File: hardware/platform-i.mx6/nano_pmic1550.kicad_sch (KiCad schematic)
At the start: 57 parts, among them J5 CAN, Q1 2SK3018, U4 AP1509, U6 PF1550

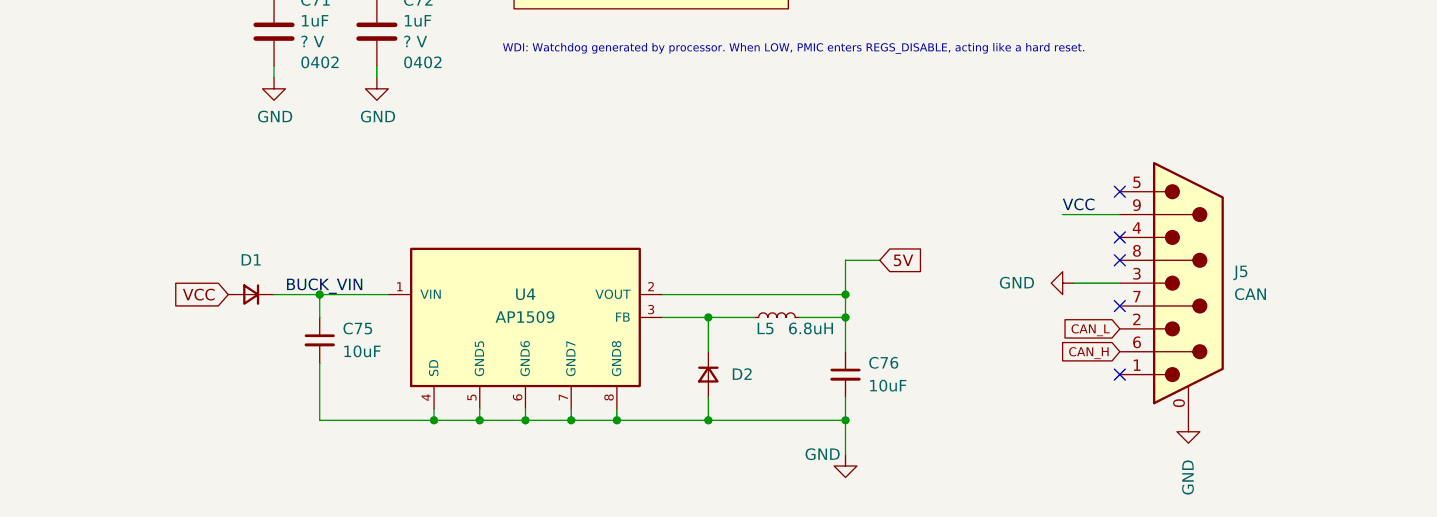
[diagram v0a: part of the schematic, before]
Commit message: Start reworking imx board into the new form factor
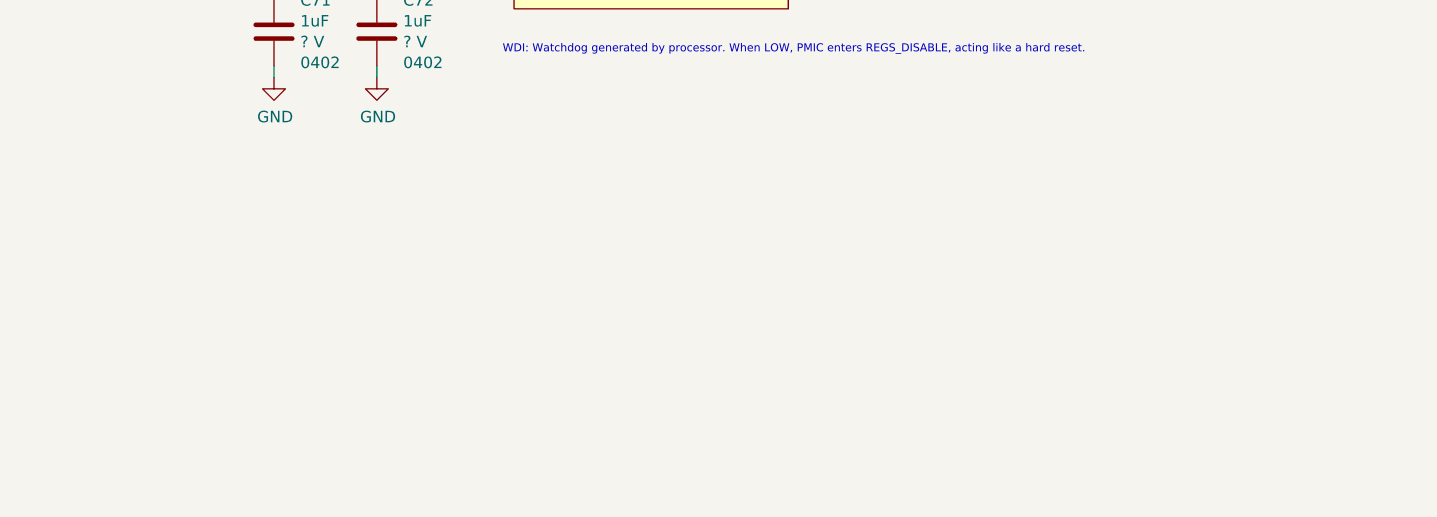
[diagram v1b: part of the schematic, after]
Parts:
- removed C75, C76: 10uF, Capacitor_SMD:C_0805_2012Metric_Pad1.18x1.45mm_HandSolder, symbol Device:C_Small
- removed D1, D2: D_Small, Diode_SMD:D_SOD-123, symbol Device:D_Small
- removed J5: CAN, Connector_Dsub:DSUB-9_Female_Horizontal_P2.77x2.84mm_EdgePinOffset4.94mm_Housed_MountingHolesOffset7.48mm, symbol Connector:DB9_Male_MountingHoles
- removed L5: 6.8uH, Inductor_SMD:L_Bourns_SRN6045TA, symbol Device:L_Small
- removed U4: AP1509, Package_SO:SOP-8_3.9x4.9mm_P1.27mm, symbol AP1509-50SG-13:AP1509-50SG-13
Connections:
- no-connect marks 6 -> 1
